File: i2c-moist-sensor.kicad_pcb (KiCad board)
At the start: 4 copper layers, 18 x 149 mm, 24 parts, among them IC1 ATTINY441-SSU, P1 CONN_02X03, P2 CONN_01X04, X1 16MHz

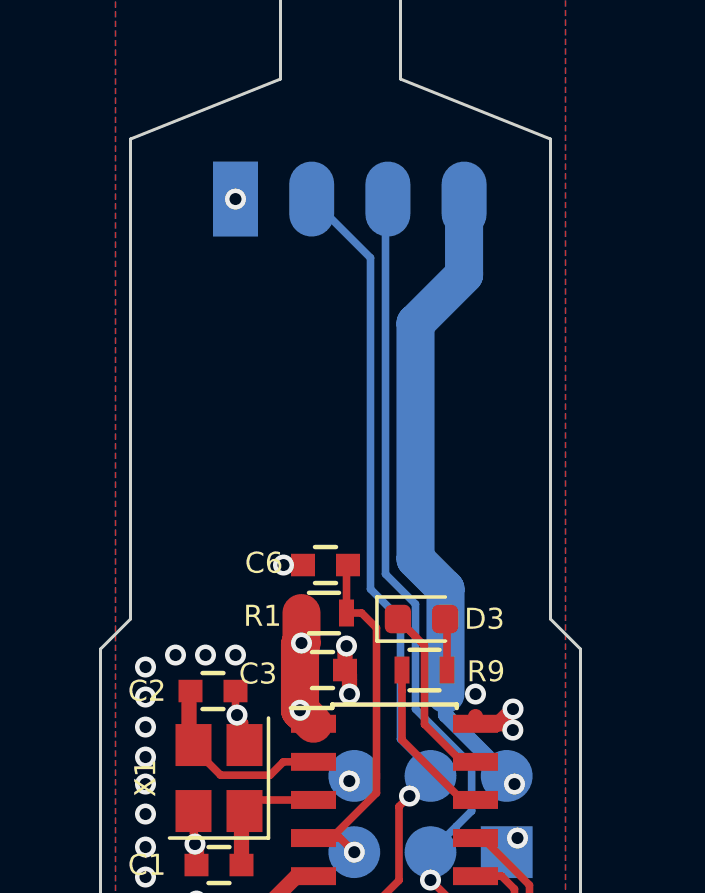
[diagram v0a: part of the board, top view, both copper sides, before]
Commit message: Add Qwiic connectors
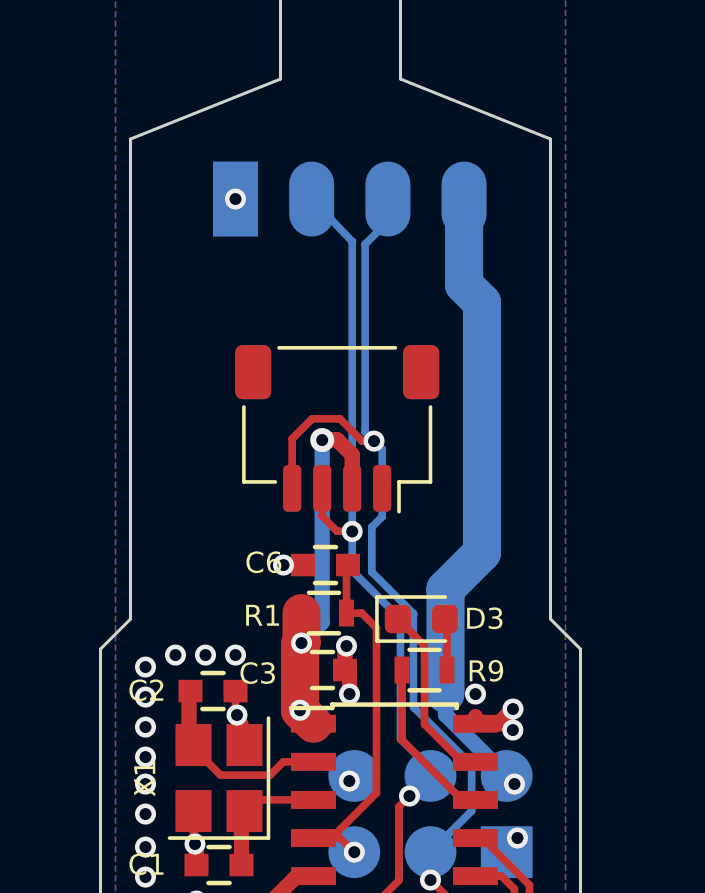
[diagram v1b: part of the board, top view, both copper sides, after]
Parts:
- added J1: QWIIC_CONNECTORJS-1MM, Connector_JST:JST_SH_SM04B-SRSS-TB_1x04-1MP_P1.00mm_Horizontal, F.Cu at (94.9, 30.1)
- added J2: QWIIC_CONNECTORJS-1MM, Connector_JST:JST_SH_SM04B-SRSS-TB_1x04-1MP_P1.00mm_Horizontal, B.Cu at (94.9, 30.1)
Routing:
- net VCC: track 33.8 -> 42.9 mm, vias 3 -> 4
- net /SCK/SCL: track 26.9 -> 32.7 mm, vias 1 -> 2
- net /MOSI/SDA: track 28.6 -> 30.8 mm, vias 1 -> 2

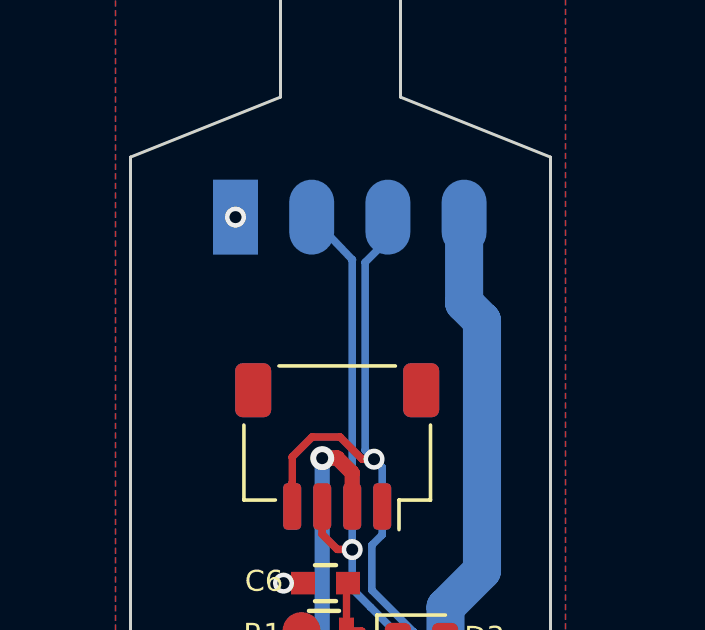
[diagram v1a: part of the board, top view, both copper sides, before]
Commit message: Add Qwiic logo above connector on front of PCB
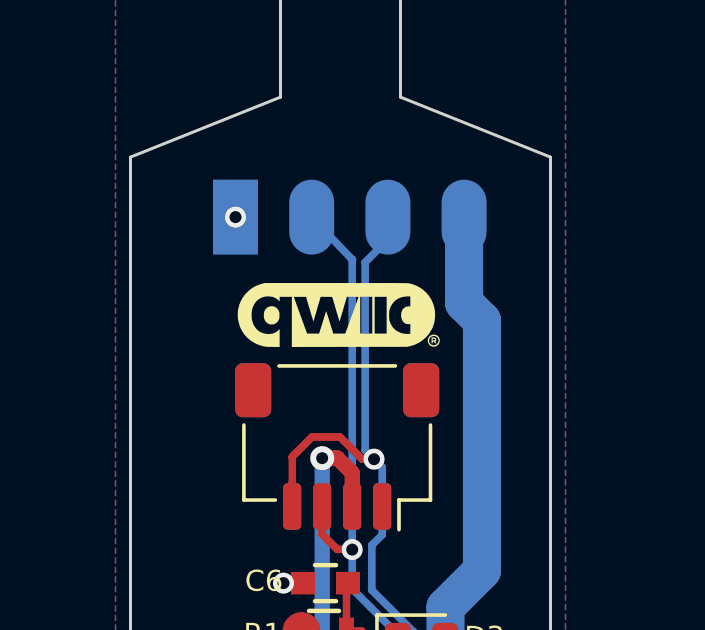
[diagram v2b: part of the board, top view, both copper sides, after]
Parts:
- added G***: LOGO, qwiic_logo:qwiic_logo, F.Cu at (94.9, 25.7)
